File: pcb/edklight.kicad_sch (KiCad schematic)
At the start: 24 parts, among them J1 MotorIn, J2 ToLcd, J3 RearLight, J4 Fr Light, J5 2 But Ctrl, Q1 ZXMP4A16G, Q2 BSP89, Q3 BSP89, Q4 ZXMP4A16G, Q5 BSP89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

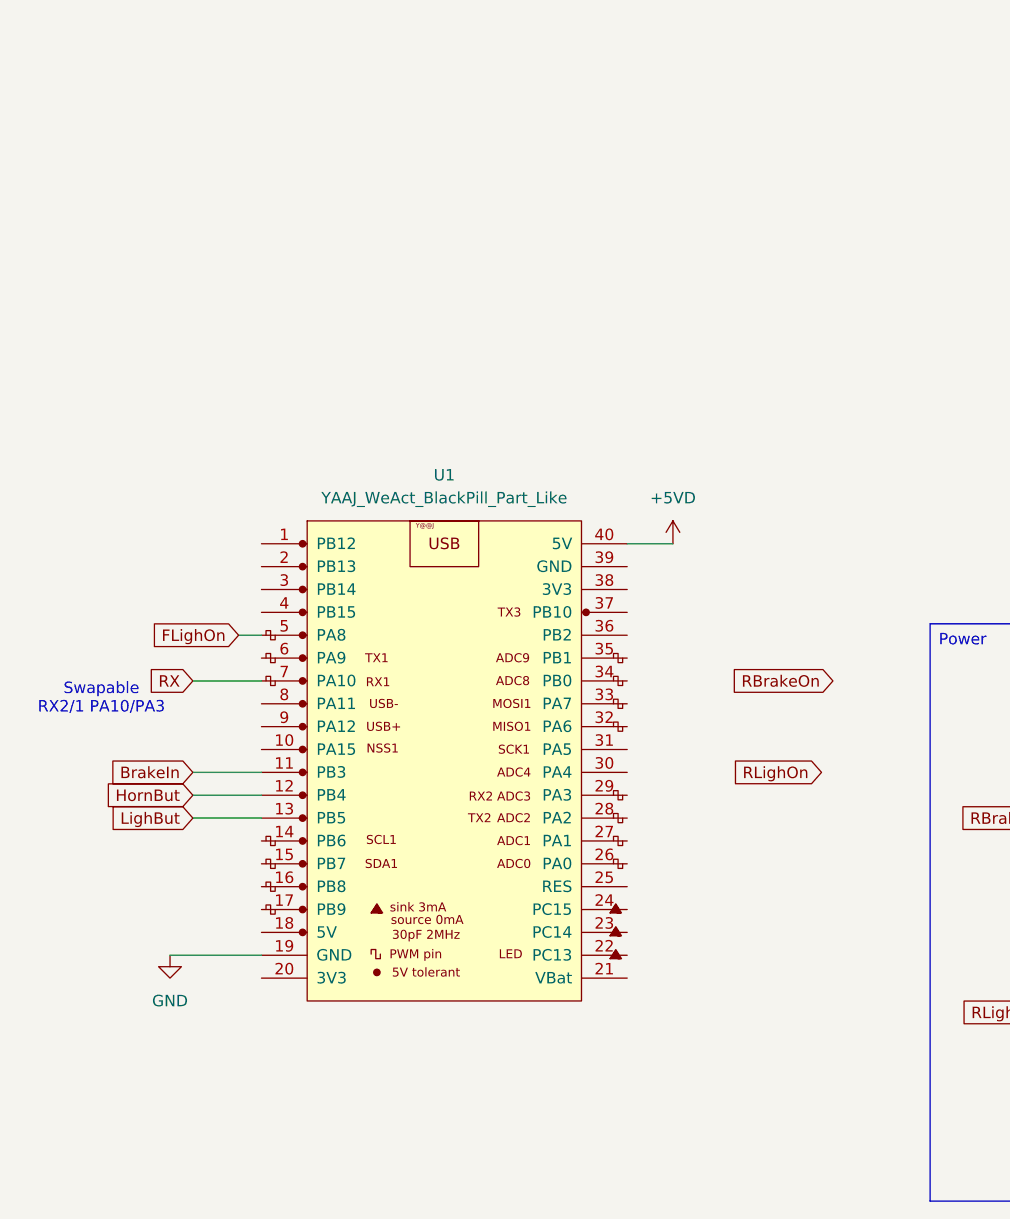
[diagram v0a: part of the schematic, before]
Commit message: note mcu brd, sch/ lib with BlackPill and Mini F103
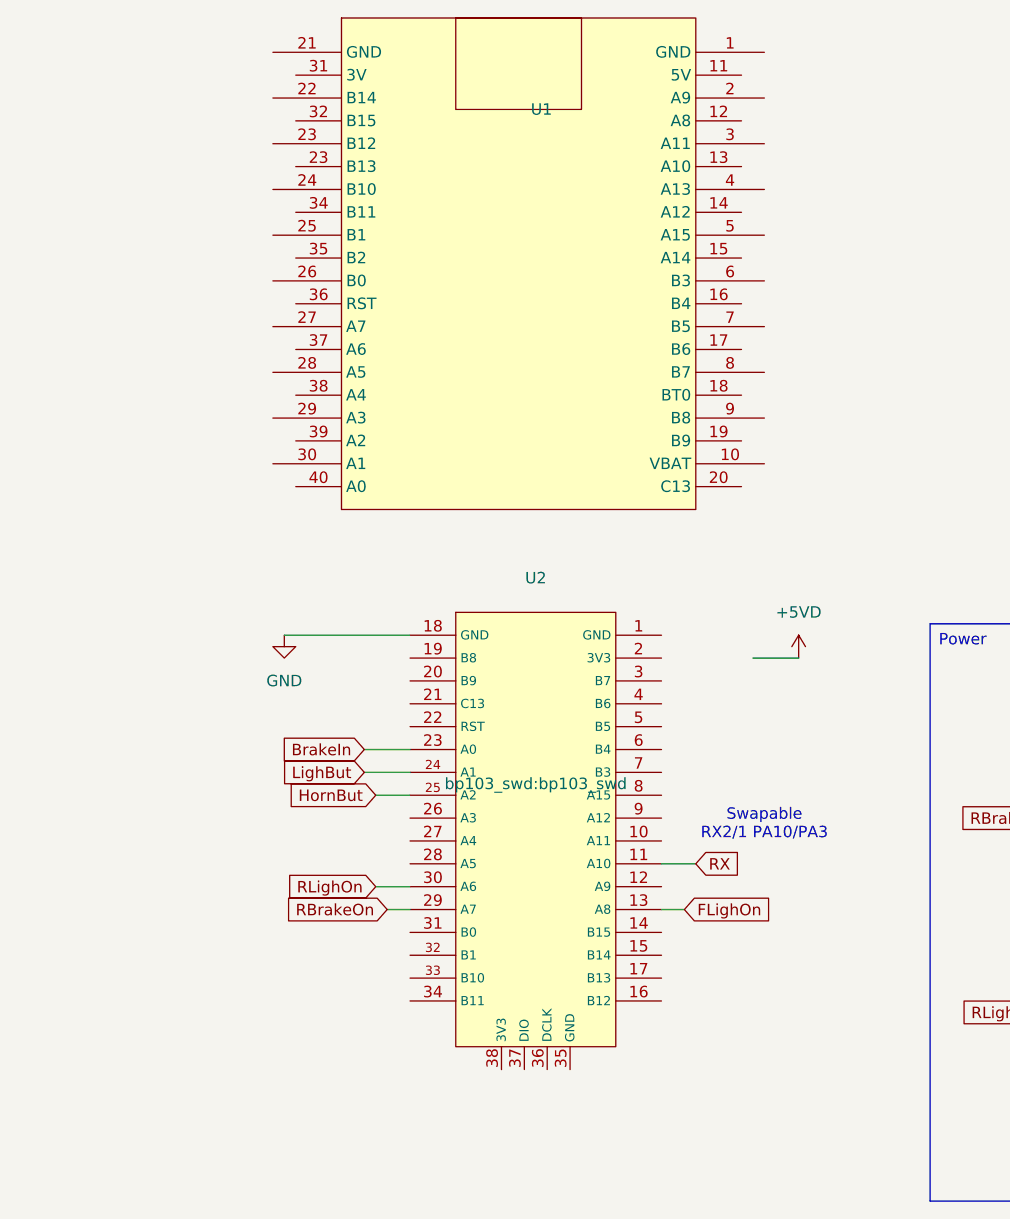
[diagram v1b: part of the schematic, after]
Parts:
- removed U1: YAAJ_WeAct_BlackPill_Part_Like, Footprints:YAAJ_BluePill_1, symbol YAAJ_WeAct_BlackPill_Part_Like:YAAJ_WeAct_BlackPill_Part_Like
- added U1: ~, bp103_swd:MiniF103, symbol bp103:MinDevF103
- added U2: ~, bp103_swd:bp103_swd, symbol bp103:bp103_swd
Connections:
- net BrakeIn: now also U2.23 (A0)
- net FLighOn: now also U2.13 (A8)
- net GND: now also U2.18 (GND)
- net HornBut: now also U2.25 (A2)
- net LighBut: now also U2.24 (A1)
- net RBrakeOn: now also U2.29 (A7)
- net RLighOn: now also U2.30 (A6)
- net RX: now also U2.11 (A10)

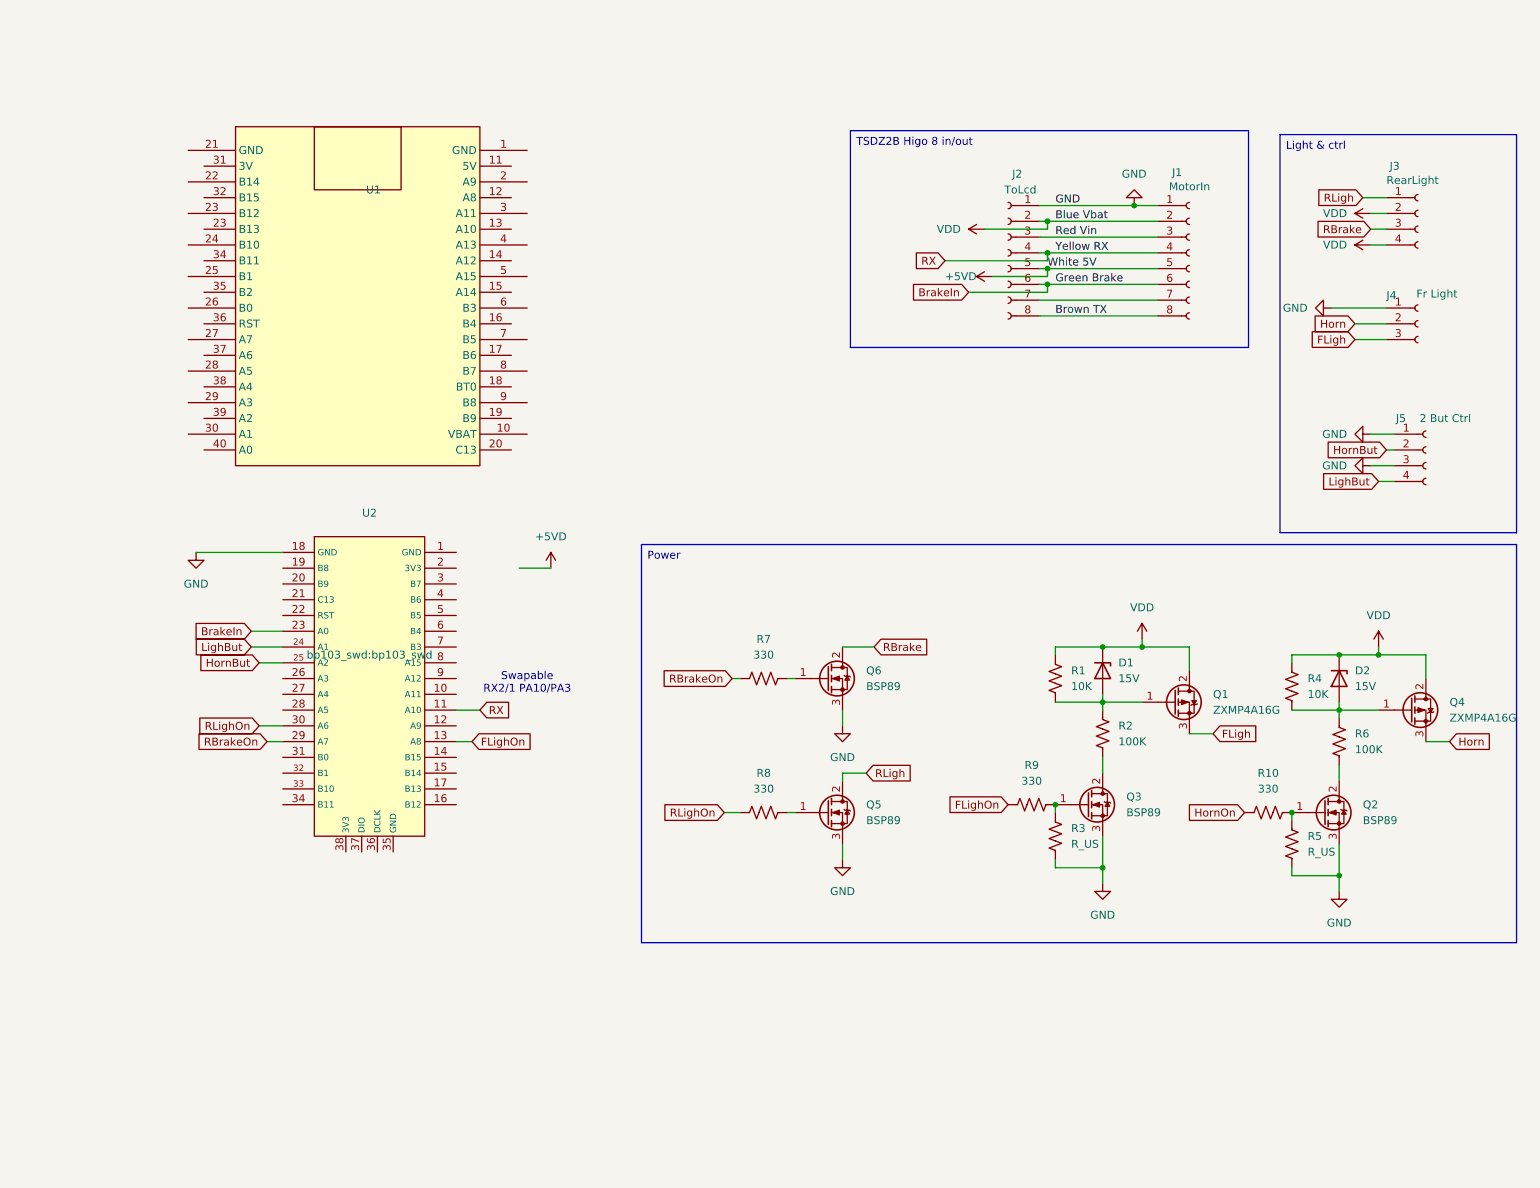
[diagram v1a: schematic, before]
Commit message: pcb swicth to mini f103 updtae higo ,single pad for wire conection
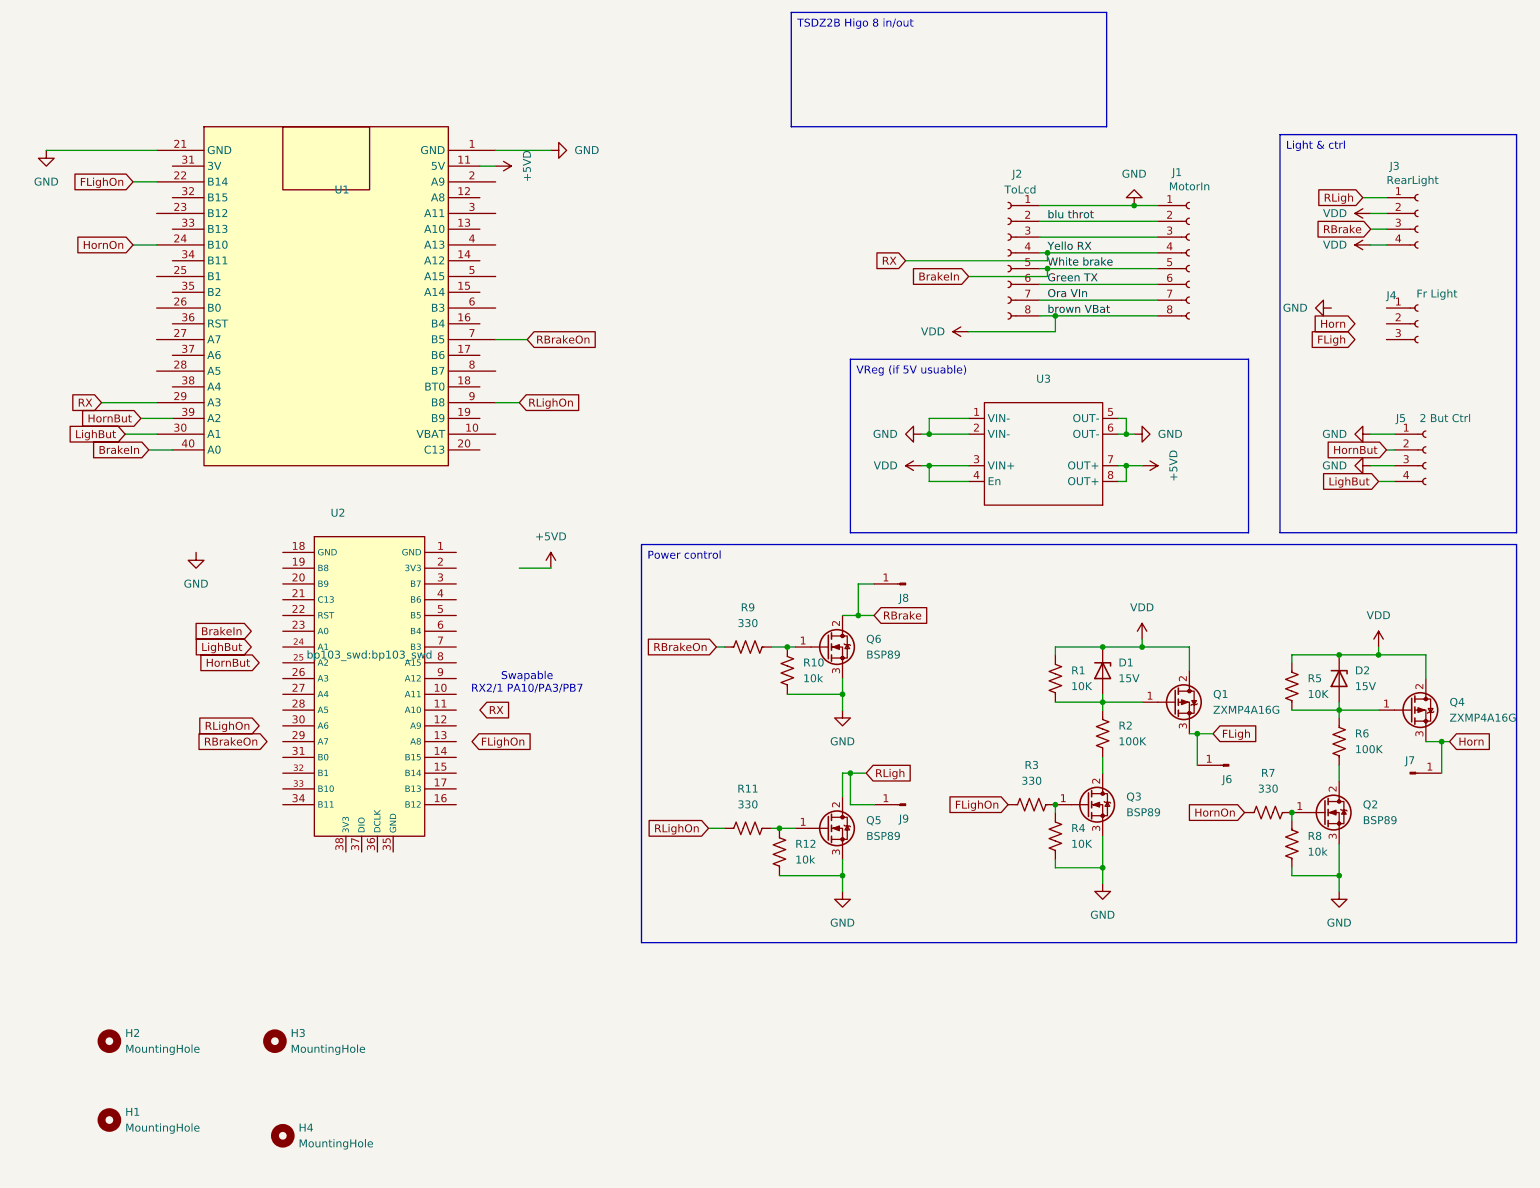
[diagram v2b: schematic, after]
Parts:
- added H1, H2, H3, H4: MountingHole, MountingHole:MountingHole_2.7mm_M2.5_DIN965, symbol Mechanical:MountingHole
- added J6, J7, J8, J9: Conn_01x01_Pin, Connector_PinHeader_2.54mm:PinHeader_1x01_P2.54mm_Vertical, symbol Connector:Conn_01x01_Pin
- added R10, R12: 10k, Resistor_THT:R_Axial_DIN0204_L3.6mm_D1.6mm_P5.08mm_Horizontal, symbol Device:R_US
- added U3: ~, bp103_swd:dce003, symbol bp103:DCE003
- D1: footprint Diode_THT:D_A-405_P2.54mm_Vertical_AnodeUp -> Diode_THT:D_A-405_P2.54mm_Vertical_KathodeUp
- R11: renamed from R8; footprint Resistor_THT:R_Axial_DIN0207_L6.3mm_D2.5mm_P7.62mm_Horizontal -> Resistor_THT:R_Axial_DIN0204_L3.6mm_D1.6mm_P7.62mm_Horizontal
- R2, R6: footprint Resistor_THT:R_Axial_DIN0207_L6.3mm_D2.5mm_P7.62mm_Horizontal -> Resistor_THT:R_Axial_DIN0204_L3.6mm_D1.6mm_P7.62mm_Horizontal
- R3: renamed from R9; footprint Resistor_THT:R_Axial_DIN0207_L6.3mm_D2.5mm_P7.62mm_Horizontal -> Resistor_THT:R_Axial_DIN0204_L3.6mm_D1.6mm_P7.62mm_Horizontal
- R4: renamed from R3; value R_US -> 10K; footprint Resistor_THT:R_Axial_DIN0207_L6.3mm_D2.5mm_P5.08mm_Vertical -> Resistor_THT:R_Axial_DIN0204_L3.6mm_D1.6mm_P5.08mm_Vertical
- R7: renamed from R10; footprint Resistor_THT:R_Axial_DIN0207_L6.3mm_D2.5mm_P7.62mm_Horizontal -> Resistor_THT:R_Axial_DIN0204_L3.6mm_D1.6mm_P7.62mm_Horizontal
- R8: renamed from R5; value R_US -> 10k; footprint Resistor_THT:R_Axial_DIN0207_L6.3mm_D2.5mm_P5.08mm_Vertical -> Resistor_THT:R_Axial_DIN0204_L3.6mm_D1.6mm_P5.08mm_Vertical
- R9: renamed from R7; footprint Resistor_THT:R_Axial_DIN0207_L6.3mm_D2.5mm_P7.62mm_Horizontal -> Resistor_THT:R_Axial_DIN0204_L3.6mm_D1.6mm_P7.62mm_Horizontal
- renumbered R4 to R5
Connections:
- net Brown TX is gone; now on net VDD: J1.8 (Pin_8), J2.8 (Pin_8)
- net +5VD: now also U1.11 (5V), U3.7 (OUT+), U3.8 (OUT+); no longer J1.5 (Pin_5), J2.5 (Pin_5)
- net BrakeIn: now also J1.5 (Pin_5), J2.5 (Pin_5), U1.40 (A0); no longer J1.6 (Pin_6), J2.6 (Pin_6), U2.23 (A0)
- net FLigh: now also J6.1 (Pin_1); no longer J4.3 (Pin_3)
- net FLighOn: now also U1.22 (B14); no longer U2.13 (A8)
- net GND: now also U1.1 (GND), U1.21 (GND), R10.2, R12.2, U3.1 (VIN-), U3.2 (VIN-), U3.5 (OUT-), U3.6 (OUT-); no longer J4.1 (Pin_1), U2.18 (GND)
- net Horn: now also J7.1 (Pin_1); no longer J4.2 (Pin_2)
- net HornBut: now also U1.39 (A2); no longer U2.25 (A2)
- net HornOn: now also U1.24 (B10)
- net LighBut: now also U1.30 (A1); no longer U2.24 (A1)
- net RBrake: now also J8.1 (Pin_1)
- net RBrakeOn: now also U1.7 (B5); no longer U2.29 (A7)
- net RLigh: now also J9.1 (Pin_1)
- net RLighOn: now also U1.9 (B8); no longer U2.30 (A6)
- net RX: now also U1.29 (A3); no longer U2.11 (A10)
- net VDD: now also U3.3 (VIN+), U3.4 (En); no longer J1.2 (Pin_2), J2.2 (Pin_2)
- net at Q6.1 (G), R9.2: now also R10.1
- net at Q5.1 (G), R11.2: now also R12.1
- net Ora VIn: now reaches J1.7 (Pin_7), J2.7 (Pin_7)
- net Red Vin: no longer names the net of J1.3 (Pin_3), J2.3 (Pin_3)
- new net Green TX: J1.6 (Pin_6), J2.6 (Pin_6)
- new net blu throt: J1.2 (Pin_2), J2.2 (Pin_2)
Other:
- note added: "Swapable RX2/1 PA10/PA3/PB7"
- note removed: "Swapable RX2/1 PA10/PA3"
- moved on the sheet: Q5, Q6, R11, R9, U1

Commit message: md udpate higo8 and brake addition , try chn pwm
use of timer chn may help moving light to different mcu pin that would
help pcb routin or proto wiring (no crossing shorter wire)
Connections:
- net RBrake: no longer J3.3 (Pin_3)
- net RLigh: no longer J3.1 (Pin_1)
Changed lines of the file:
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@@
 	(text_box "TSDZ2B Higo 8 in/out"
 		(exclude_from_sim no)
-		(at 137.795 5.715 0)
-		(size 50.8 18.415)
+		(at 147.955 25.4 0)
+		(size 63.5 34.925)
 		(margins 0.9525 0.9525 0.9525 0.9525)
 		(stroke
@@
 	(wire
 		(pts
-			(xy 229.87 35.56) (xy 233.68 35.56)
-		)
-		(stroke
-			(width 0)
-			(type default)
-		)
-	)
-	(wire
-		(pts
 			(xy 218.44 110.49) (xy 218.44 109.22)
 		)
@@
 		)
 		(stroke
-			(width 0)
-			(type default)
-		)
-	)
-	(wire
-		(pts
-			(xy 231.14 40.64) (xy 233.68 40.64)
-		)
-		(stroke

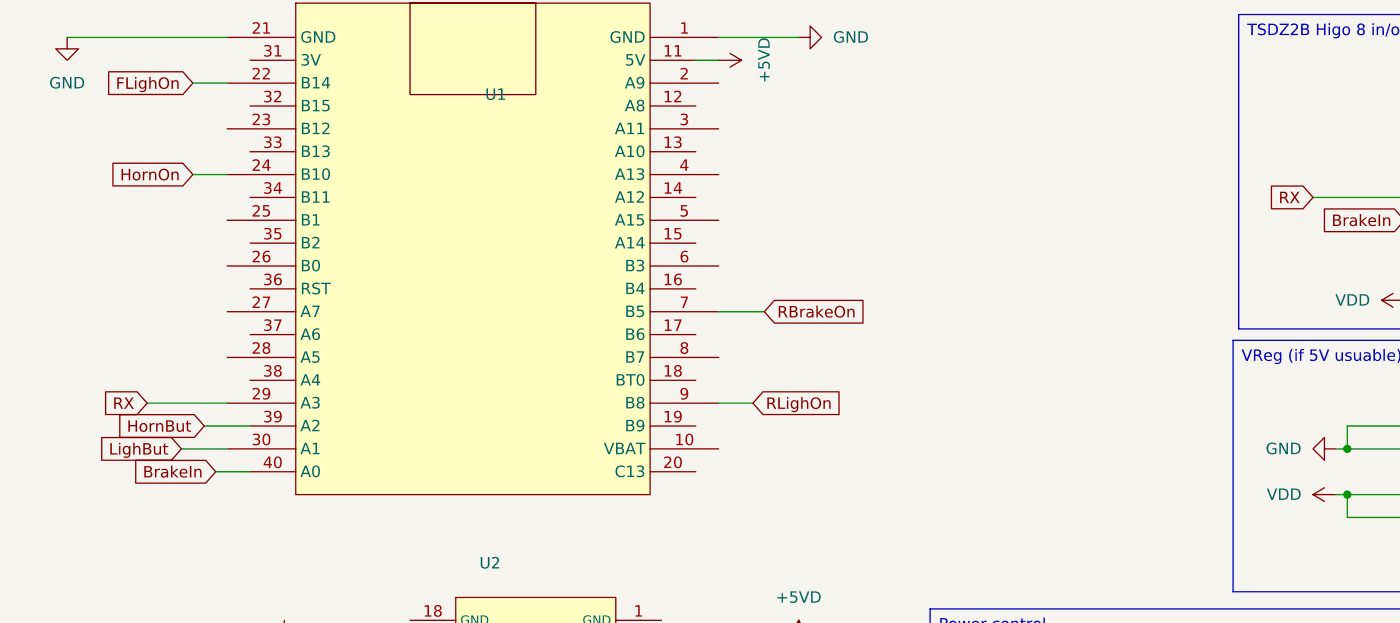
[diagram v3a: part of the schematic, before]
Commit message: pcb : chg button pin   add debounce capacitor
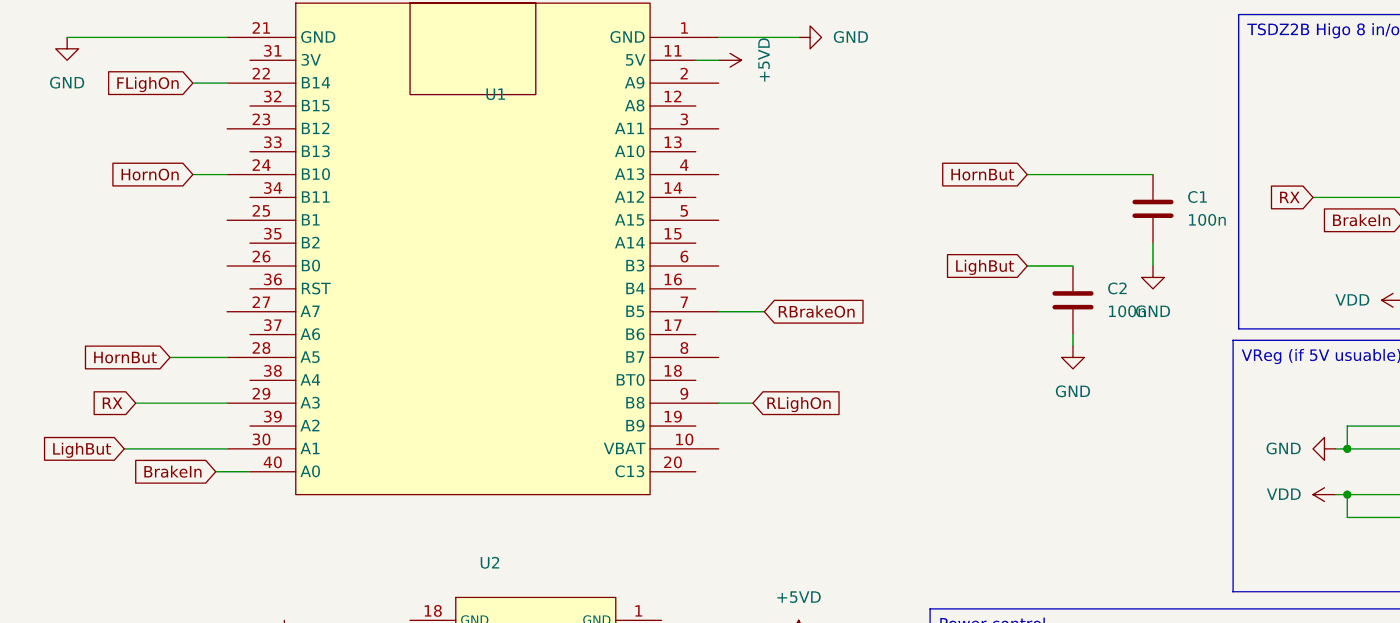
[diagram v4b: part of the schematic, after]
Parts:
- added C1, C2: 100n, Capacitor_THT:C_Disc_D4.3mm_W1.9mm_P5.00mm, symbol Device:C
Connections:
- net GND: now also C1.2, C2.2
- net HornBut: now also U1.28 (A5), C1.1; no longer U1.39 (A2)
- net LighBut: now also C2.1
